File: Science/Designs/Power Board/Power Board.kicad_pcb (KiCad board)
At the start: 2 copper layers, 114.3 x 90.2 mm, 25 parts, among them P1 PWR_IN, P2 MOTOR_PWR_OUT, P3 MAIN_PWR_OUT, P4 I2C, P5 MOTOR_SW, P6 REG_12V, P7 REG_5V, U1 INA219, U2 INA219, U3 INA219

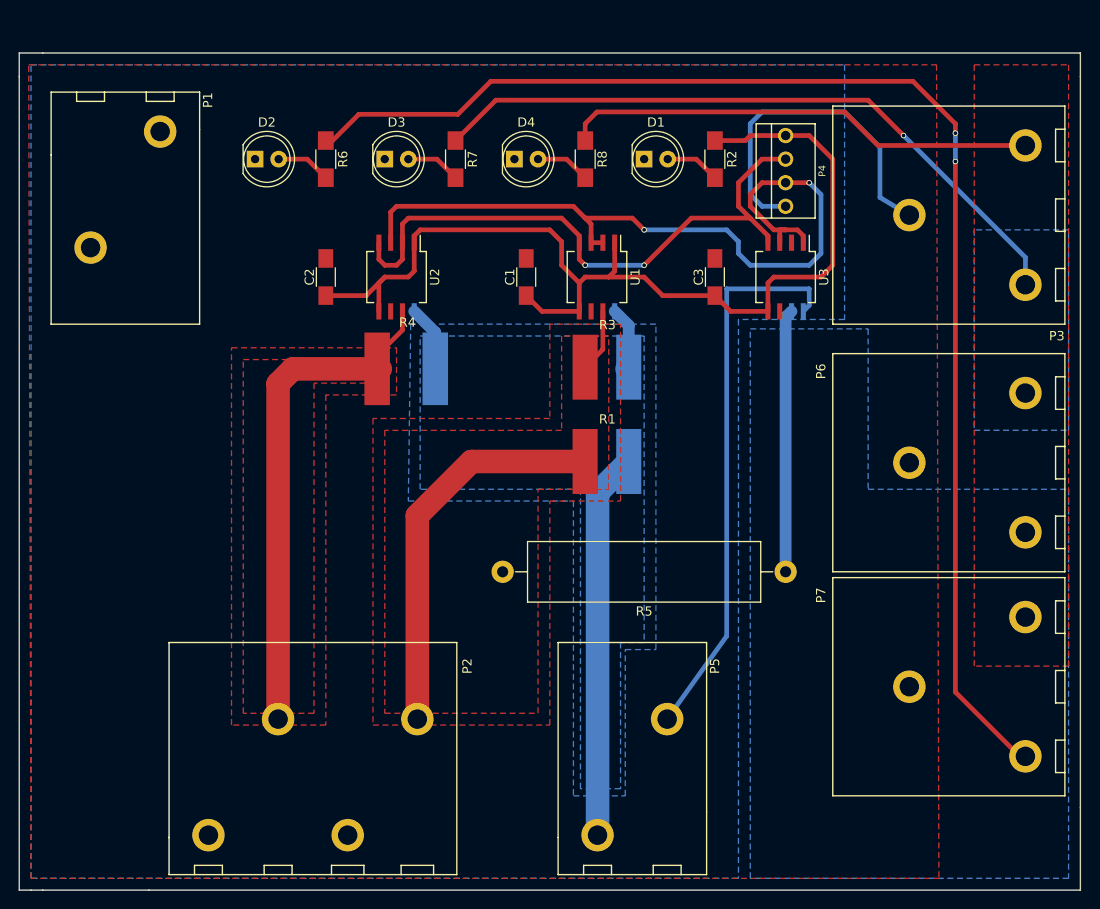
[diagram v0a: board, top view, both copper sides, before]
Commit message: Added CAD files for 3-PIN molex connector
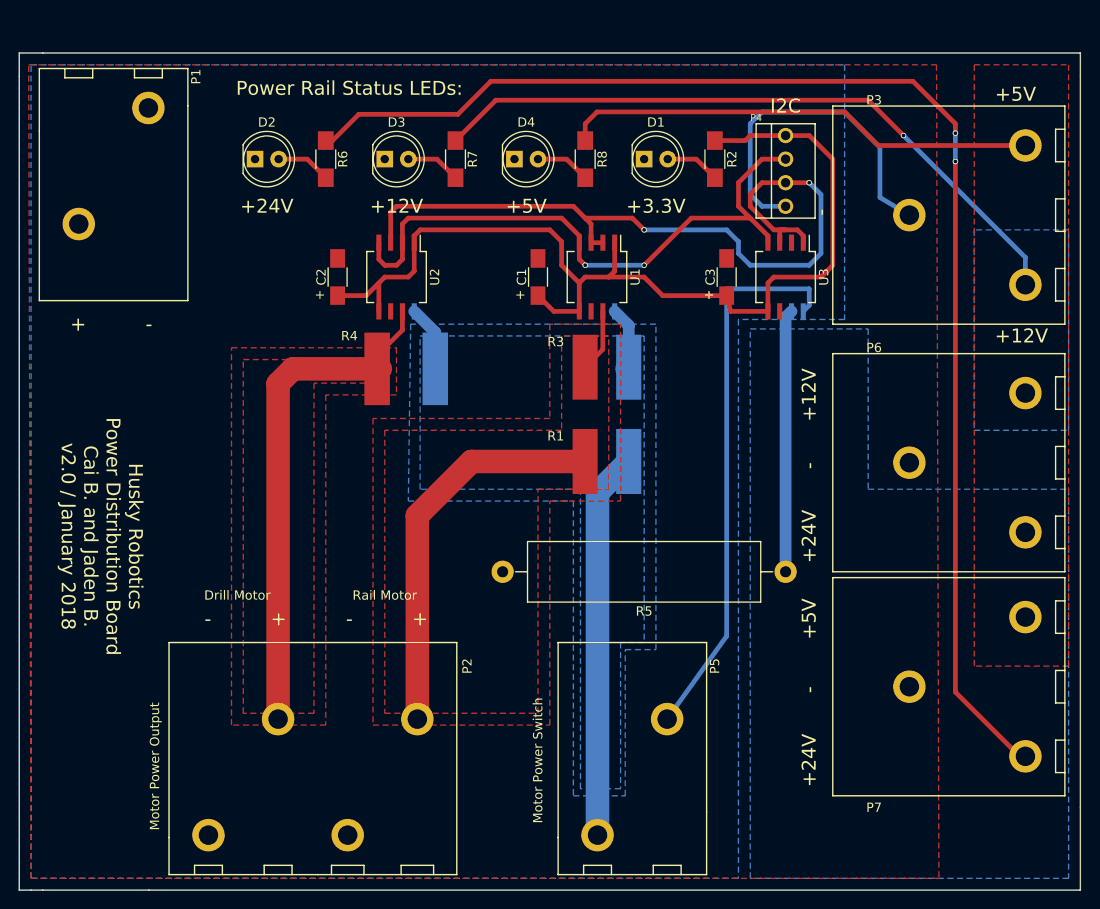
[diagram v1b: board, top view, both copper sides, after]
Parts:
- moved P1 2.84 mm to (83.8, 54.6)
- moved C3 1.27 mm to (149.9, 52.1)
- moved C2 1.27 mm to (108.0, 52.1)
- moved C1 1.27 mm to (129.5, 52.1)
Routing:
- net +3V3: track 113.4 -> 110.0 mm
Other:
- board text added: "+"
- board text added: "+12V"
- board text added: "+24V"
- board text added: "+3.3V"
- board text added: "+5V"
- board text added: "-"
- board text added: "Drill Motor"
- board text added: "Husky Robotics Power Distribution Board Cai B. and Jaden B. v2.0 / January 2018"
- board text added: "I2C"
- board text added: "Motor Power Output"
- board text added: "Motor Power Switch"
- board text added: "Power Rail Status LEDs:"
- board text added: "Rail Motor"

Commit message: Updated footprints
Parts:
- U1, U2, U3: footprint Housings_SOIC:SO-8_5.3x6.2mm_Pitch1.27mm -> ScienceFootprints:SO-8_5.3x6.2mm_Pitch1.27mm

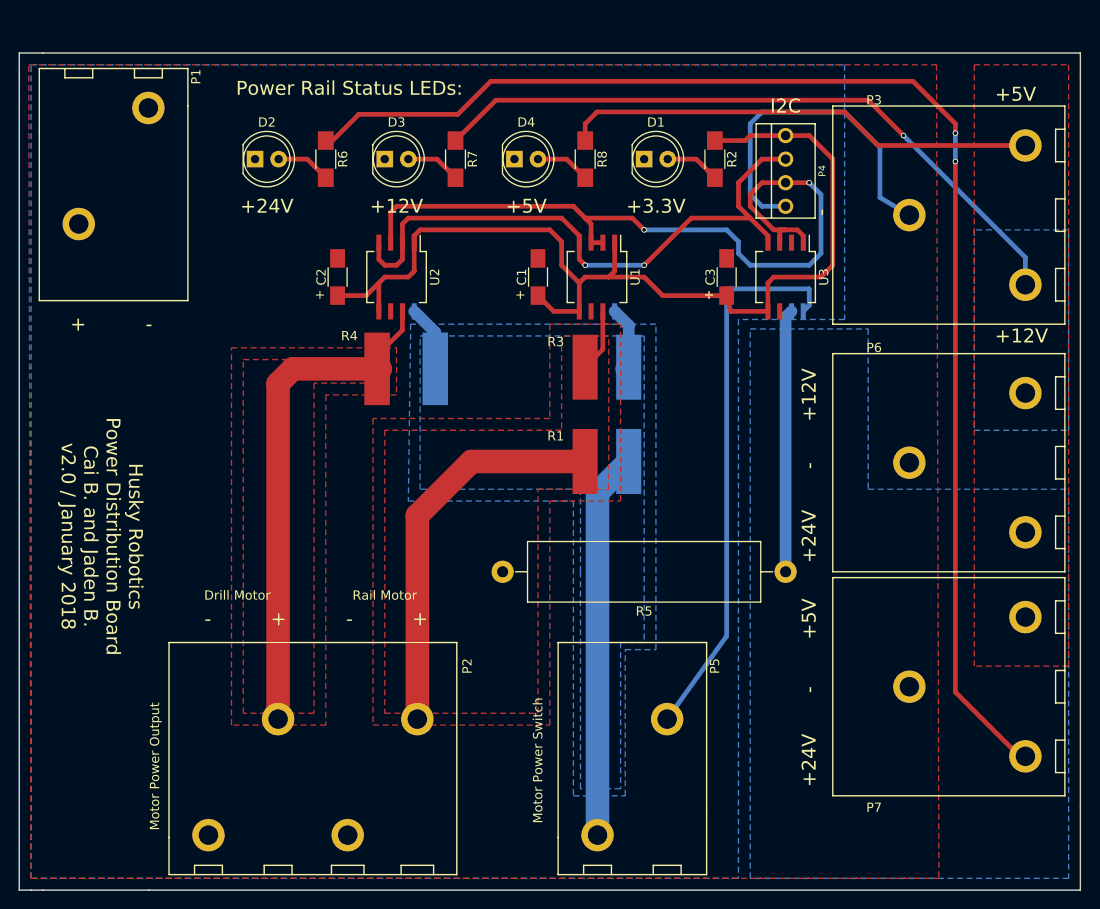
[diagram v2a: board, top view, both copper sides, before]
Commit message: Added mounting holes
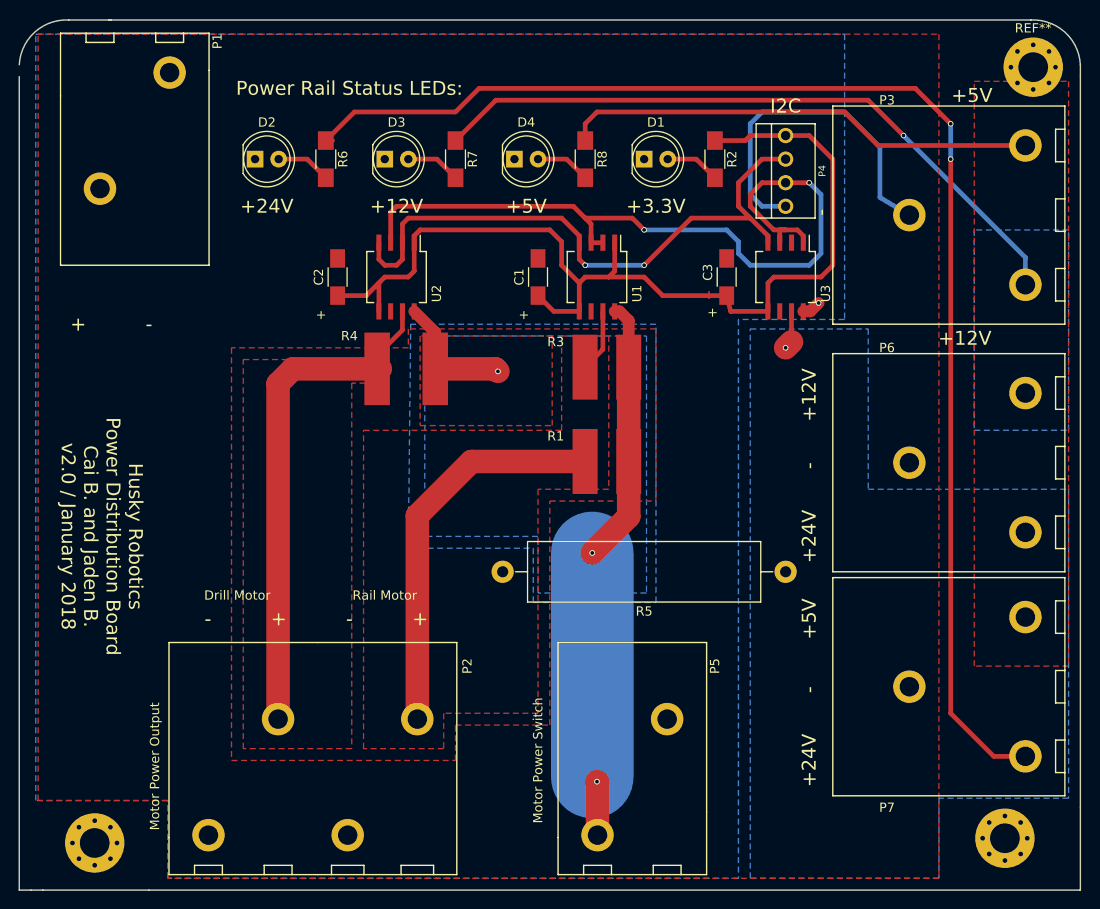
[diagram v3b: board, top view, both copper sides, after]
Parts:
- added REF**: MountingHole_3.2mm_M3_Pad_Via, Mounting_Holes:MountingHole_3.2mm_M3_Pad_Via, F.Cu at (81.8, 113.0)
- added REF**: MountingHole_3.2mm_M3_Pad_Via, Mounting_Holes:MountingHole_3.2mm_M3_Pad_Via, F.Cu at (179.8, 112.5)
- added REF**: MountingHole_3.2mm_M3_Pad_Via, Mounting_Holes:MountingHole_3.2mm_M3_Pad_Via, F.Cu at (182.9, 29.5)
- moved P1 4.44 mm to (86.1, 50.8)
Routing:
- net /24V_IN: track 60.7 -> 2.73 mm, vias 0 -> 1
- net +24V: track 173.7 -> 151.7 mm, vias 2 -> 3
- net Net-(P5-Pad1): track 58.8 -> 73.2 mm, vias 0 -> 3
- added copper zone on F.Cu, net Net-(P5-Pad1)
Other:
- board size 114.3 x 90.2 mm -> 114.3 x 93.7 mm

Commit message: Done for the nigtht.
Good progress!
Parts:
- added REF**: MountingHole_3.2mm_M3_Pad_Via, Mounting_Holes:MountingHole_3.2mm_M3_Pad_Via, F.Cu at (99.3, 49.8)
- moved REF** 3.09 mm to (182.9, 113.0)
- moved REF** 3.05 mm to (78.7, 113.0)
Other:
- outline, holes or cut-outs redrawn
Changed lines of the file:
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@@
     (links 60)
     (no_connects 0)
-    (area 73.584999 27.864999 188.035001 118.185001)
+    (area 73.584999 24.308999 188.035001 118.185001)
     (thickness 1.6)
-    (drawings 42)
+    (drawings 38)
     (tracks 172)
     (zones 0)
-    (modules 28)
+    (modules 29)
     (nets 16)
   )
   (page A4)
   (layers
-    (0 F.Cu signal)
-    (31 B.Cu signal)
+    (0 F.Cu signal hide)
+    (31 B.Cu signal hide)
     (32 B.Adhes user hide)
     (33 F.Adhes user hide)
@@
   )
   (module Mounting_Holes:MountingHole_3.2mm_M3_Pad_Via (layer F.Cu)
-    (at 81.788 113.03)
+    (at 78.74 113.03)
     (descr "Mounting Hole 3.2mm, M3")
     (tags "mounting hole 3.2mm m3")
@@
       (effects (font (size 1 1) (thickness 0.15)))
     )
-    (fp_text value MountingHole_3.2mm_M3_Pad_Via (at 0 4.2) (layer F.Fab)
+    (fp_text value MountingHole_3.2mm_M3_Pad_Via (at 0 4.2) (layer F.Fab) hide
       (effects (font (size 1 1) (thickness 0.15)))
     )
@@
   )
   (module Mounting_Holes:MountingHole_3.2mm_M3_Pad_Via (layer F.Cu)
-    (at 179.832 112.522)
+    (at 182.88 113.03)
     (descr "Mounting Hole 3.2mm, M3")
     (tags "mounting hole 3.2mm m3")
@@
       (effects (font (size 1 1) (thickness 0.15)))
     )
-    (fp_text value MountingHole_3.2mm_M3_Pad_Via (at 0 4.2) (layer F.Fab)
+    (fp_text value MountingHole_3.2mm_M3_Pad_Via (at 0 4.2) (layer F.Fab) hide
       (effects (font (size 1 1) (thickness 0.15)))
     )
@@
     (tags "mounting hole 3.2mm m3")
     (attr virtual)
-    (fp_text reference REF** (at 0 -4.2) (layer F.SilkS)
-      (effects (font (size 1 1) (thickness 0.15)))
-    )
-    (fp_text value MountingHole_3.2mm_M3_Pad_Via (at 0 4.2) (layer F.Fab)
+    (fp_text reference REF** (at 0 -4.2) (layer F.SilkS) hide
+      (effects (font (size 1 1) (thickness 0.15)))
+    )
+    (fp_text value MountingHole_3.2mm_M3_Pad_Via (at 0 4.2) (layer F.Fab) hide
       (effects (font (size 1 1) (thickness 0.15)))
     )
@@
     (pad "" thru_hole circle (at 1.697056 -1.697056) (size 0.8 0.8) (drill 0.5) (layers *.Cu *.Mask))
   )
-  (gr_line (start 78.994 24.384) (end 83.566 24.384) (angle 90) (layer Edge.Cuts) (width 0.15))
-  (gr_arc (start 78.74 29.464) (end 73.66 29.21) (angle 90) (layer Edge.Cuts) (width 0.15))
-  (gr_line (start 182.626 24.384) (end 83.312 24.384) (angle 90) (layer Edge.Cuts) (width 0.15))
-  (gr_line (start 187.96 30.48) (end 187.96 29.21) (angle 90) (layer Edge.Cuts) (width 0.15))
-  (gr_arc (start 182.88 29.464) (end 182.626 24.384) (angle 90) (layer Edge.Cuts) (width 0.15))
+  (module Mounting_Holes:MountingHole_3.2mm_M3_Pad_Via (layer F.Cu)
+    (at 99.314 49.784)
+    (descr "Mounting Hole 3.2mm, M3")
+    (tags "mounting hole 3.2mm m3")
+    (attr virtual)
+    (fp_text reference REF** (at 0.254 4.826) (layer F.SilkS) hide
+      (effects (font (size 1 1) (thickness 0.15)))
+    )
+    (fp_text value MountingHole_3.2mm_M3_Pad_Via (at 0 6.604) (layer F.Fab) hide
+      (effects (font (size 1 1) (thickness 0.15)))
+    )
+    (fp_text user %R (at 0.3 0) (layer F.Fab)
+      (effects (font (size 1 1) (thickness 0.15)))
+    )
+    (fp_circle (center 0 0) (end 3.2 0) (layer Cmts.User) (width 0.15))
+    (fp_circle (center 0 0) (end 3.45 0) (layer F.CrtYd) (width 0.05))
+    (pad 1 thru_hole circle (at 0 0) (size 6.4 6.4) (drill 3.2) (layers *.Cu *.Mask))
+    (pad "" thru_hole circle (at 2.4 0) (size 0.8 0.8) (drill 0.5) (layers *.Cu *.Mask))
+    (pad "" thru_hole circle (at 1.697056 1.697056) (size 0.8 0.8) (drill 0.5) (layers *.Cu *.Mask))
+    (pad "" thru_hole circle (at 0 2.4) (size 0.8 0.8) (drill 0.5) (layers *.Cu *.Mask))
+    (pad "" thru_hole circle (at -1.697056 1.697056) (size 0.8 0.8) (drill 0.5) (layers *.Cu *.Mask))
+    (pad "" thru_hole circle (at -2.4 0) (size 0.8 0.8) (drill 0.5) (layers *.Cu *.Mask))
+    (pad "" thru_hole circle (at -1.697056 -1.697056) (size 0.8 0.8) (drill 0.5) (layers *.Cu *.Mask))
+    (pad "" thru_hole circle (at 0 -2.4) (size 0.8 0.8) (drill 0.5) (layers *.Cu *.Mask))
+    (pad "" thru_hole circle (at 1.697056 -1.697056) (size 0.8 0.8) (drill 0.5) (layers *.Cu *.Mask))
+  )
+  (gr_line (start 182.88 118.11) (end 78.74 118.11) (angle 90) (layer Edge.Cuts) (width 0.15))
+  (gr_line (start 187.96 29.464) (end 187.96 113.03) (angle 90) (layer Edge.Cuts) (width 0.15))
+  (gr_line (start 78.74 24.384) (end 182.88 24.384) (angle 90) (layer Edge.Cuts) (width 0.15))
+  (gr_line (start 73.66 113.03) (end 73.66 29.464) (angle 90) (layer Edge.Cuts) (width 0.15))
+  (gr_arc (start 78.74 29.464) (end 73.66 29.464) (angle 90) (layer Edge.Cuts) (width 0.15))
+  (gr_arc (start 182.88 29.464) (end 182.88 24.384) (angle 90) (layer Edge.Cuts) (width 0.15))
+  (gr_arc (start 182.88 113.03) (end 187.96 113.03) (angle 90) (layer Edge.Cuts) (width 0.15))
+  (gr_arc (start 78.74 113.03) (end 78.74 118.11) (angle 90) (layer Edge.Cuts) (width 0.15))
   (gr_text "Rail Motor" (at 113.03 86.36) (layer F.SilkS)
     (effects (font (size 1 1) (thickness 0.2)))
@@
     (effects (font (size 1.5 1.5) (thickness 0.3)))
   )
-  (gr_text "Power Rail Status LEDs:" (at 109.22 31.75) (layer F.SilkS)
+  (gr_text "Power Rail Status LEDs:" (at 110.236 31.496) (layer F.SilkS)
     (effects (font (size 1.5 1.5) (thickness 0.3)))
   )
@@
     (effects (font (size 1.5 1.5) (thickness 0.3)))
   )
-  (gr_text - (at 87.63 57.15) (layer F.SilkS)
-    (effects (font (size 1.5 1.5) (thickness 0.3)))
-  )
-  (gr_text + (at 80.01 57.15) (layer F.SilkS)
+  (gr_text - (at 90.17 52.07) (layer F.SilkS)
+    (effects (font (size 1.5 1.5) (thickness 0.3)))
+  )
+  (gr_text + (at 82.042 52.07) (layer F.SilkS)
     (effects (font (size 1.5 1.5) (thickness 0.3)))
   )
@@
     (effects (font (size 1.5 1.5) (thickness 0.3)))
   )
-  (gr_line (start 74.93 118.11) (end 76.2 118.11) (angle 90) (layer Edge.Cuts) (width 0.15))
-  (gr_line (start 74.93 118.11) (end 73.66 118.11) (angle 90) (layer Edge.Cuts) (width 0.15))
-  (gr_line (start 73.66 118.11) (end 73.66 30.48) (angle 90) (layer Edge.Cuts) (width 0.15))
-  (gr_line (start 87.63 118.11) (end 76.2 118.11) (angle 90) (layer Edge.Cuts) (width 0.15))
-  (gr_line (start 187.96 118.11) (end 87.63 118.11) (angle 90) (layer Edge.Cuts) (width 0.15))
-  (gr_line (start 187.96 109.22) (end 187.96 118.11) (angle 90) (layer Edge.Cuts) (width 0.15))
-  (gr_line (start 187.96 30.48) (end 187.96 109.22) (angle 90) (layer Edge.Cuts) (width 0.15))
   (segment (start 107.95 54.07) (end 111.03 54.07) (width 0.508) (layer F.Cu) (net 1))
   (segment (start 111.03 54.07) (end 112.395 52.705) (width 0.508) (layer F.Cu) (net 1))
@@
       )
     )
+    (polygon
+      (pts        (xy 103.124 53.34) (xy 103.124 45.974) (xy 95.504 45.974) (xy 95.504 53.594) (xy 103.124 53.594)
+      )
+    )
   )
   (zone (net 7) (net_name /24V_IN) (layer B.Cu) (hatch edge 0.508)
@@
       (pts
         (xy 162.56 25.908) (xy 162.56 56.642) (xy 151.13 56.642) (xy 151.13 116.84) (xy 89.662 116.84)
-        (xy 89.662 108.458) (xy 75.438 108.458) (xy 75.438 25.908)
+        (xy 89.662 108.458) (xy 75.692 108.458) (xy 75.692 25.908)
       )
     )
@@
       (pts        (xy 115.824 57.15) (xy 115.57 81.28) (xy 129.032 81.28) (xy 129.032 87.122) (xy 133.096 87.122)
         (xy 133.096 107.95) (xy 137.922 107.95) (xy 137.922 87.122) (xy 142.24 87.122) (xy 142.24 57.15)
+      )
+    )
+    (polygon
+      (pts        (xy 103.124 45.974) (xy 103.124 53.594) (xy 95.504 53.594) (xy 95.504 45.974)
       )
     )
@@
     (polygon
       (pts
-        (xy 186.69 46.99) (xy 176.53 46.99) (xy 176.53 68.58) (xy 186.69 68.58)
+        (xy 186.69 46.99) (xy 175.006 46.99) (xy 175.006 68.58) (xy 186.69 68.58)
       )
     )
@@
     (polygon
       (pts
-        (xy 176.53 30.988) (xy 186.69 30.988) (xy 186.69 93.98) (xy 176.53 93.98)
+        (xy 175.006 30.734) (xy 186.69 30.988) (xy 186.69 98.806) (xy 175.006 98.552)
       )
     )
